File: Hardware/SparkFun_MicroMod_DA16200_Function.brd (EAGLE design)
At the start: 65 x 38 mm, 45 parts, among them J1 MICROMOD_STANDARD, J2 CORTEX_JTAG_DEBUG, U1 DA16200MOD, U2 CH340E_MSOP10, U3 3.3V

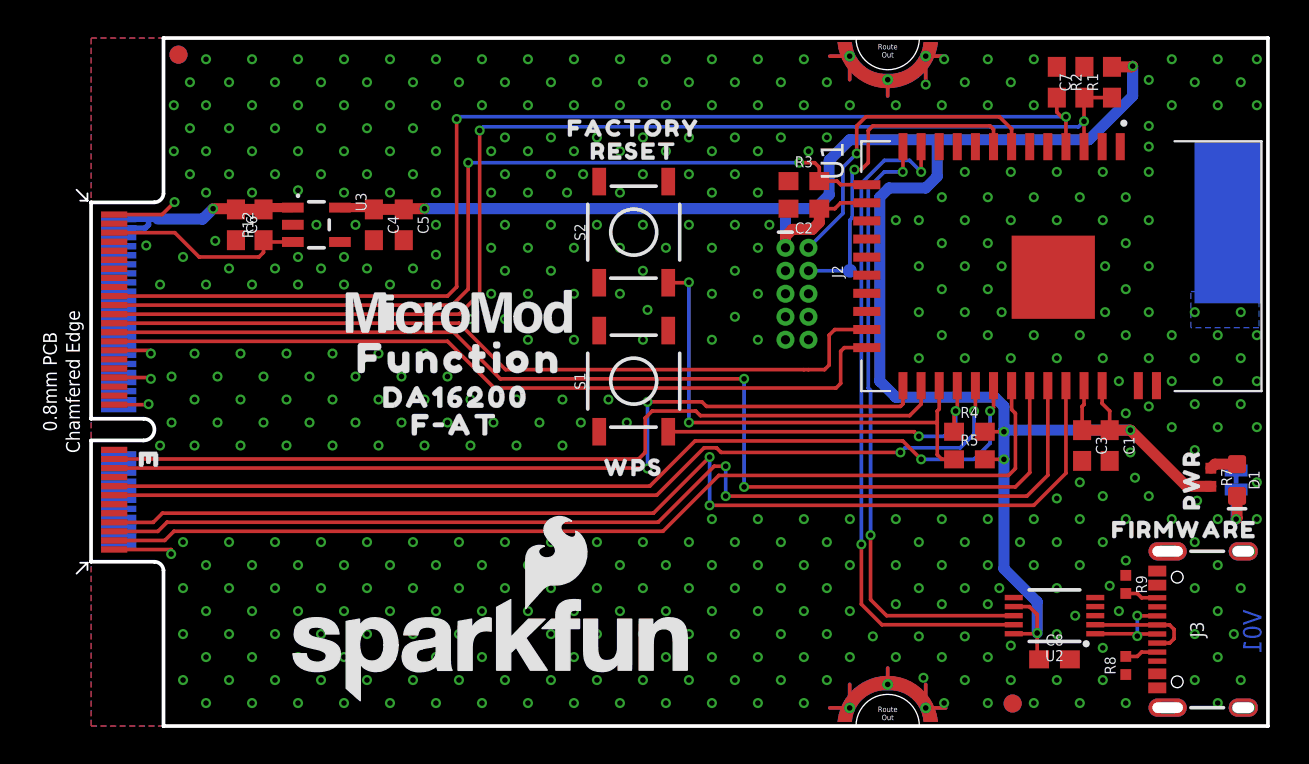
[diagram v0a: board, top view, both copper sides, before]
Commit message: Design Review Changes
Swapped U1RX/TX
Corrected SCL/SDA
Added a few more vias on the PCB
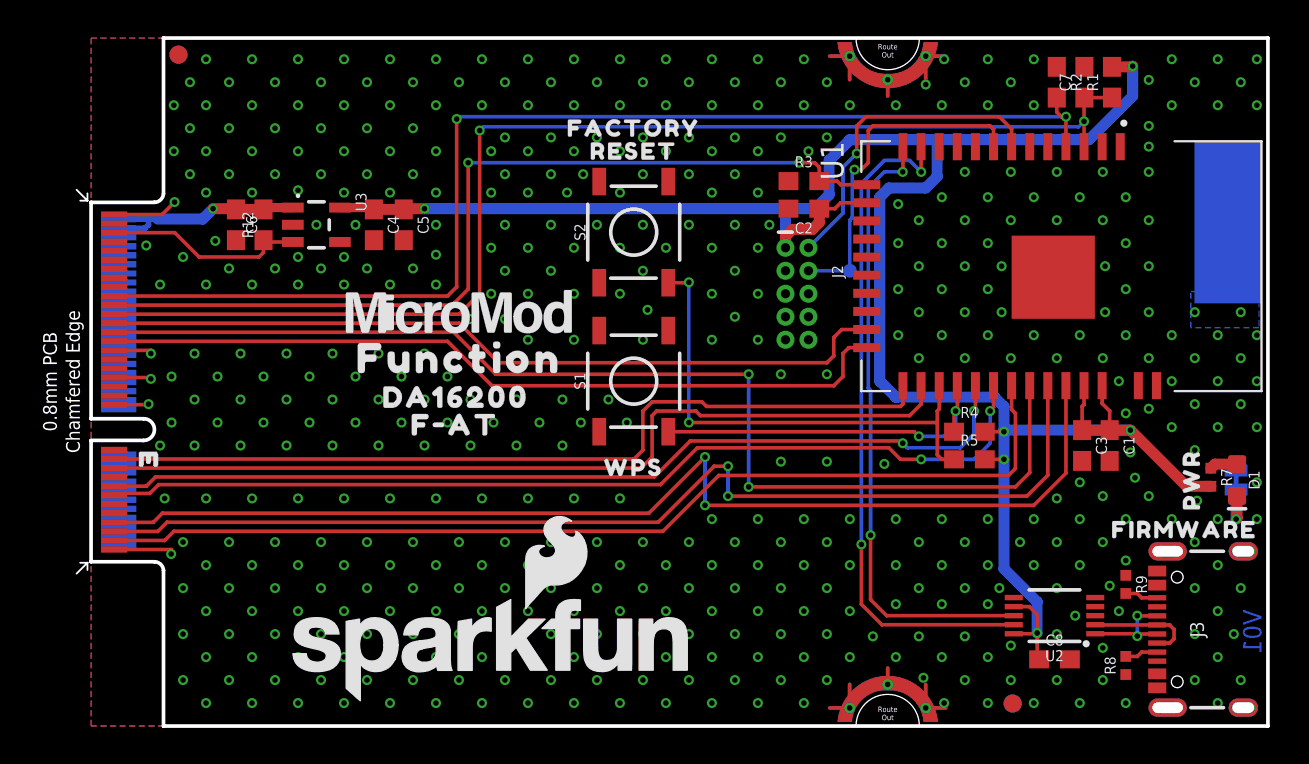
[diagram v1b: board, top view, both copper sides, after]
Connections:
- net CS renamed !CS!
- net SCL: now also J1.21; no longer J1.19
- net SDA: now also J1.19; no longer J1.21
- net U1RXI: now also J1.15; no longer J1.13
- net U1TXO: now also J1.13; no longer J1.15
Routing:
- net SCL: track 48.4 -> 47.3 mm, vias 2 -> 0
- net GPIOA11: track 44.5 -> 43.8 mm
- net GND: vias 476 -> 495

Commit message: Added Ordering Instructions
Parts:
- added LOGO3: SPECIAL_INSTRUCTIONS-ORDERING, SparkFun-Aesthetics:ORDERING_INSTRUCTIONS
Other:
- board text added: "0.8mm PCB ENIG Finish 45 degree chamfered edge"
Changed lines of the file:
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@@
 <dimension x1="4" y1="38" x2="65" y2="38" x3="34.5" y3="41" textsize="1.016" textratio="15" layer="47"/>
 <dimension x1="0" y1="9.075" x2="65" y2="9" x3="32.486146875" y3="-2.969409375" textsize="1.016" textratio="15" layer="47" visible="yes"/>
+<text x="86.36" y="29.21" size="1.778" layer="51" font="vector" ratio="15">0.8mm PCB
+ENIG Finish
+45 degree chamfered edge</text>
 </plain>
 <attributes>
@@
 <attribute name="VALUE" x="16.51" y="27.686" size="0.6096" layer="27" font="vector" ratio="20" rot="R270" align="top-center"/>
 </element>
+<element name="LOGO3" library="SparkFun-Aesthetics" package="ORDERING_INSTRUCTIONS" value="SPECIAL_INSTRUCTIONS-ORDERING" x="85.09" y="46.99" smashed="yes"/>
 </elements>
 <signals>

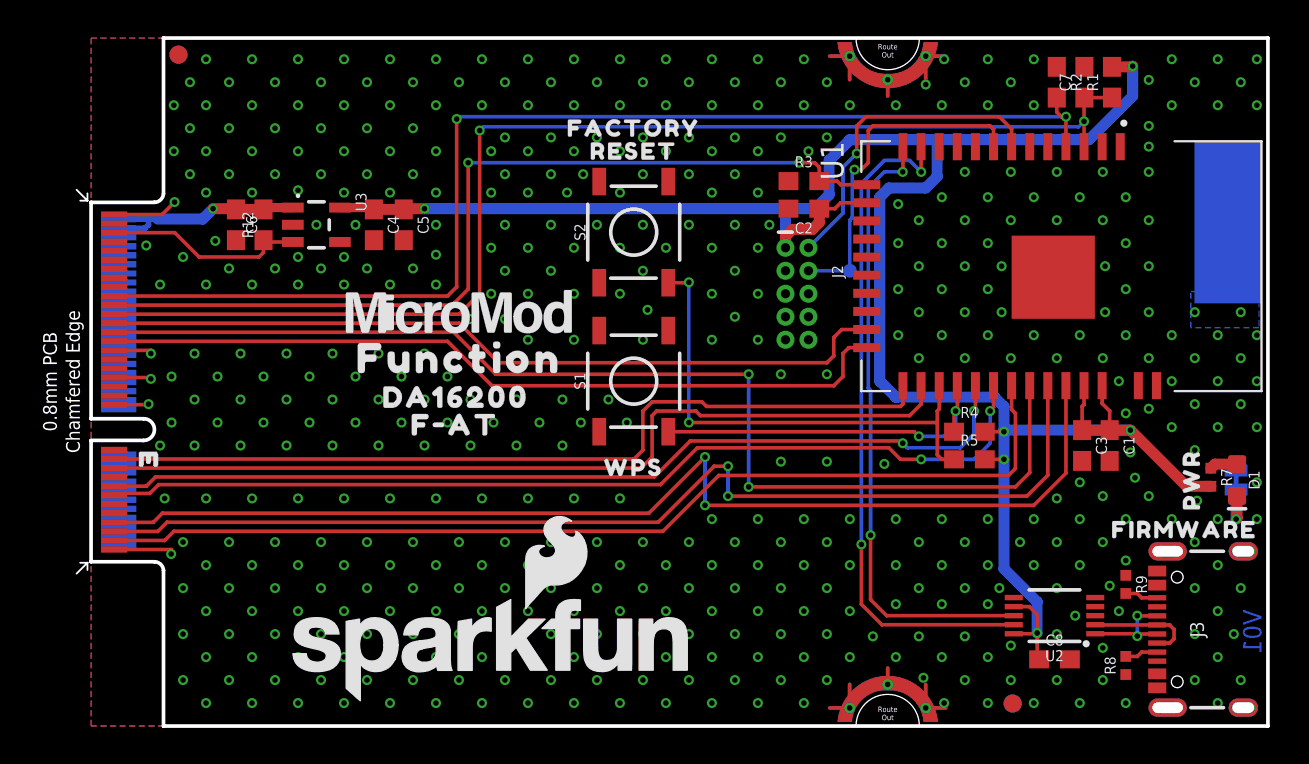
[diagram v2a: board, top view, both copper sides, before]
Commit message: V10
Added EEPROM, I2C Pullups
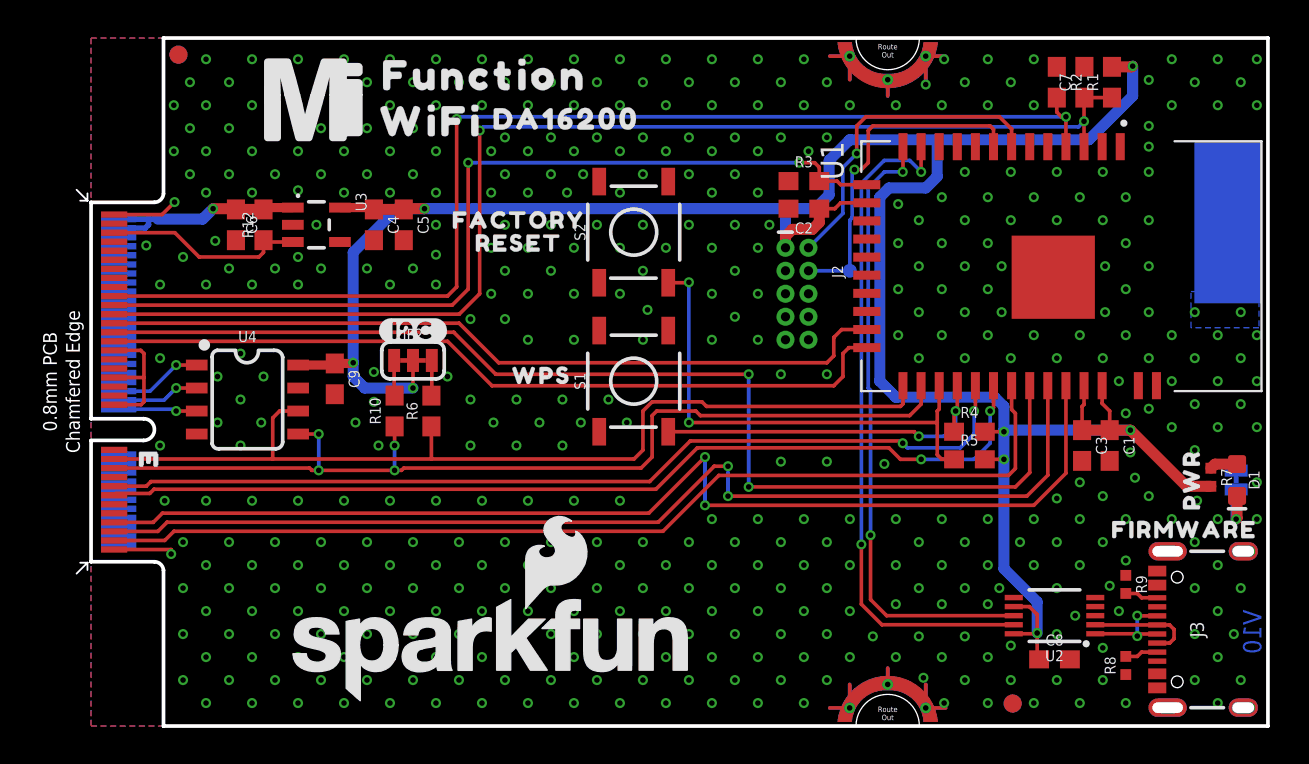
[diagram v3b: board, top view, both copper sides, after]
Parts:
- removed FRAME1: FRAME-LETTER, SparkFun-Aesthetics:CREATIVE_COMMONS
- removed U$10: (no value), SparkFun-MicroMod:MICROMOD_LOGO_.5
- added C9: 0.1uF, SparkFun-Capacitors:0603
- added FRAME2: FRAME-LEDGER, SparkFun-Aesthetics:CREATIVE_COMMONS
- added JP2: JUMPER-SMT_3_2-NC_TRACE_SILK, SparkFun-Jumpers:SMT-JUMPER_3_2-NC_TRACE_SILK
- added R10, R6: 4.7k, SparkFun-Resistors:0603
- added U$11: (no value), output:#I2C#0
- added U$12: (no value), SparkFun-MicroMod:MICROMOD_MI_LOGO_1
- added U4: EEPROM, SparkFun-IC-Memory:SO08
- U$6: device output:F#AT0 -> output:WIFI0
- moved U$6 16.8 mm to (18.8, 33.4)
- moved U$5 16.5 mm to (26.2, 33.5)
- moved U$4 15.7 mm to (21.7, 35.9)
- moved U$8 8.13 mm to (23.6, 27.9)
- moved U$9 8.13 mm to (23.6, 26.7)
- moved LOGO3 8.03 mm to (77.5, 44.5)
- moved U$7 7.18 mm to (24.9, 19.4)
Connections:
- removed net SCL: J1.21, U1.24
- removed net SDA: J1.19, U1.25
- new net I2C_SCL: J1.21, R6.1, U1.24, U4.6
- new net I2C_SDA: J1.19, R10.1, U1.25, U4.5
- new net N$1: J1.36, U4.1
- new net N$13: JP2.1, R10.2
- new net N$14: JP2.3, R6.2
- new net N$8: J1.32, U4.3
- new net N$9: J1.34, U4.2
- net 3.3V: now also C9.1, JP2.2, U4.8
- net GND: now also C9.2, U4.4, U4.7
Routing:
- net I2C_SDA: track 0.00 -> 54.3 mm, vias 0 -> 4
- net I2C_SCL: track 0.00 -> 52.9 mm
- net SDA: track 48.6 -> 0.00 mm
- net SCL: track 47.3 -> 0.00 mm
- net 3.3V: track 123.4 -> 143.5 mm, vias 6 -> 8
- net N$1: track 0.00 -> 4.91 mm, vias 0 -> 1
- net N$9: track 0.00 -> 4.59 mm, vias 0 -> 1
- net N$8: track 0.00 -> 4.35 mm, vias 0 -> 1
- net N$14: track 0.00 -> 1.97 mm
- net N$13: track 0.00 -> 1.97 mm
- net GND: track 24.6 -> 26.1 mm, vias 495 -> 470
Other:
- board text added: "V10"
- board text removed: "V01"

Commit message: V10 update
Added diodes for VIN and VUSB
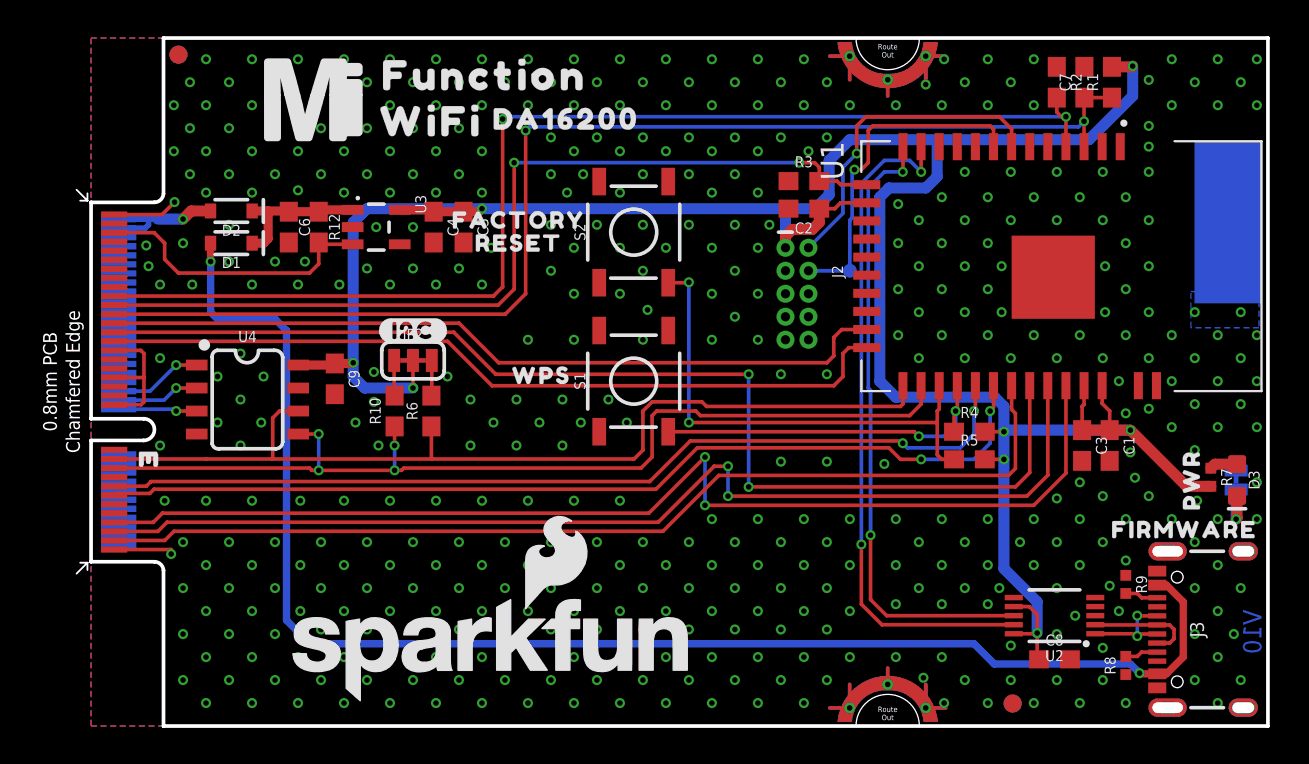
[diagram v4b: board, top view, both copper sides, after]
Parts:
- added D2: (no value), SparkFun-DiscreteSemi:SOD-323
- added D3: RED, SparkFun-MicroMod-Function:LED-0603
- D1: value RED -> (none); device SparkFun-MicroMod-Function:LED-0603 -> SparkFun-DiscreteSemi:SOD-323
- moved D1 57.1 mm to (7.75, 26.7), turned to 180 degrees
- moved C5 3.30 mm to (20.6, 27.6)
- moved U3 3.30 mm to (15.7, 27.6)
- moved C4 3.30 mm to (18.9, 27.6)
- moved R12 3.05 mm to (12.6, 27.6), turned to 270 degrees
- moved C6 2.92 mm to (10.9, 27.6)
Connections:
- new net N$3: C6.1, D1.C, D2.C, R12.1, U3.1
- new net V_USB: D1.A, J3.VBUS1, J3.VBUS2
- net EN: now also R12.2; no longer R12.1
- net N$6: now also D3.C; no longer D1.C
- net N$7: now also D3.A; no longer D1.A
- net VCC: now also D2.A; no longer C6.1, R12.2, U3.1
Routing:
- net V_USB: track 0.00 -> 80.4 mm, vias 0 -> 2
- net N$3: track 0.00 -> 8.12 mm
- net EN: track 11.2 -> 16.1 mm
- net VCC: track 12.0 -> 7.30 mm
- net 3.3V: track 143.5 -> 144.4 mm
- net GND: vias 470 -> 459

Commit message: V10 EEPROM changes
Added pullup, jumper, and MM pin map for EEPROM WP pin
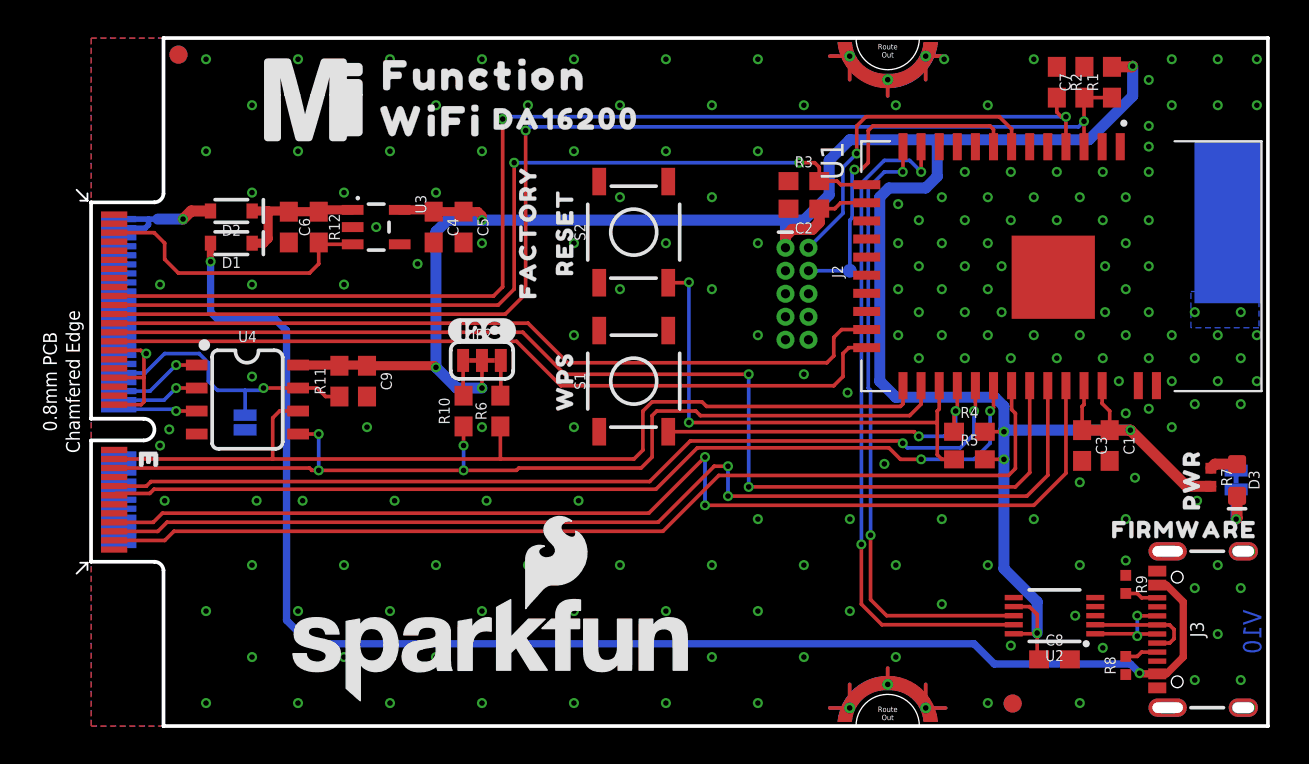
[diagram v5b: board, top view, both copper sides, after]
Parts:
- added JP3: (no value), SparkFun-Jumpers:SMT-JUMPER_2_NO_SILK
- added R11: 10k, SparkFun-Resistors:0603
- added U$10: (no value), output:#WP#0
- moved R10 3.81 mm to (20.6, 17.4)
- moved R6 3.81 mm to (22.6, 17.4)
- moved JP2 3.81 mm to (21.6, 20.2)
- moved U$11 3.81 mm to (21.6, 21.8)
- moved U$9 2.61 mm to (26.2, 27.3), turned to 90 degrees
- moved C9 1.78 mm to (15.2, 19.1)
- moved U$7 1.31 mm to (26.2, 19.1), turned to 90 degrees
- moved U$8 0.83 mm to (24.1, 27.3), turned to 90 degrees
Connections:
- new net EWP: J1.40, JP3.2, R11.1, U4.7
- net 3.3V: now also R11.2
- net GND: now also JP3.1; no longer U4.7
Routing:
- net EWP: track 0.00 -> 15.7 mm, vias 0 -> 1
- net GND: track 26.1 -> 19.1 mm, vias 459 -> 185
- net 3.3V: track 144.4 -> 142.6 mm

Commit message: Updates function board symbol, fixes text that was not vector
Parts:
- JP3: value (none) -> JUMPER-SMT_2_NO_SILK
- R1: value DNP -> (none)
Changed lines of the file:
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@@
 <drawing>
 <settings>
-<setting alwaysvectorfont="yes"/>
+<setting alwaysvectorfont="no"/>
 <setting verticaltext="up"/>
 </settings>
-<grid distance="0.05" unitdist="inch" unit="inch" style="lines" multiple="1" display="yes" altdistance="0.005" altunitdist="inch" altunit="inch"/>
+<grid distance="0.05" unitdist="inch" unit="inch" style="dots" multiple="1" display="yes" altdistance="0.005" altunitdist="inch" altunit="inch"/>
 <layers>
 <layer number="1" name="Top" color="4" fill="1" visible="yes" active="yes"/>
@@
 <layer number="14" name="Route14" color="22" fill="1" visible="no" active="no"/>
 <layer number="15" name="Route15" color="23" fill="1" visible="no" active="no"/>
-<layer number="16" name="Bottom" color="1" fill="1" visible="yes" active="yes"/>
-<layer number="17" name="Pads" color="2" fill="1" visible="yes" active="yes"/>
+<layer number="16" name="Bottom" color="3" fill="1" visible="yes" active="yes"/>
+<layer number="17" name="Pads" color="26" fill="1" visible="yes" active="yes"/>
 <layer number="18" name="Vias" color="2" fill="1" visible="yes" active="yes"/>
 <layer number="19" name="Unrouted" color="6" fill="1" visible="yes" active="yes"/>
-<layer number="20" name="Dimension" color="24" fill="1" visible="yes" active="yes"/>
+<layer number="20" name="Dimension" color="15" fill="1" visible="yes" active="yes"/>
 <layer number="21" name="tPlace" color="16" fill="1" visible="yes" active="yes"/>
 <layer number="22" name="bPlace" color="14" fill="1" visible="yes" active="yes"/>
@@
 <layer number="37" name="tTest" color="7" fill="1" visible="no" active="yes"/>
 <layer number="38" name="bTest" color="7" fill="1" visible="no" active="yes"/>
-<layer number="39" name="tKeepout" color="4" fill="11" visible="yes" active="yes"/>
+<layer number="39" name="tKeepout" color="4" fill="11" visible="no" active="yes"/>
 <layer number="40" name="bKeepout" color="1" fill="11" visible="no" active="yes"/>
 <layer number="41" name="tRestrict" color="4" fill="10" visible="no" active="yes"/>
@@
 <layer number="43" name="vRestrict" color="2" fill="10" visible="no" active="yes"/>
 <layer number="44" name="Drills" color="7" fill="1" visible="no" active="yes"/>
-<layer number="45" name="Holes" color="7" fill="1" visible="no" active="yes"/>
+<layer number="45" name="Holes" color="7" fill="1" visible="yes" active="yes"/>
 <layer number="46" name="Milling" color="3" fill="1" visible="no" active="yes"/>
-<layer number="47" name="Measures" color="7" fill="1" visible="yes" active="yes"/>
+<layer number="47" name="Measures" color="7" fill="1" visible="no" active="yes"/>
 <layer number="48" name="Document" color="7" fill="1" visible="no" active="yes"/>
-<layer number="49" name="Reference" color="7" fill="1" visible="no" active="yes"/>
+<layer number="49" name="Reference" color="13" fill="1" visible="yes" active="yes"/>
 <layer number="50" name="dxf" color="7" fill="1" visible="no" active="no"/>
 <layer number="51" name="tDocu" color="6" fill="1" visible="yes" active="yes"/>
@@
 </element>
 <element name="TP1" library="SparkFun-Connectors" package="PAD.03X.03" value="" x="41.91" y="25.146" smashed="yes" rot="MR0"/>
-<element name="R1" library="SparkFun-Resistors" package="0603" value="DNP" x="56.388" y="35.56" smashed="yes" rot="R90">
+<element name="R1" library="SparkFun-Resistors" package="0603" value=" " x="56.388" y="35.56" smashed="yes" rot="R90">
 <attribute name="NAME" x="55.626" y="35.56" size="0.6096" layer="25" font="vector" ratio="20" rot="R90" align="bottom-center"/>
 <attribute name="PROD_ID" value=" " x="57.658" y="15.24" size="1.778" layer="27" font="vector" ratio="15" rot="R90" display="off"/>
@@
 <attribute name="VALUE" x="14.478" y="19.05" size="0.6096" layer="27" font="vector" ratio="20" rot="R90" align="top-center"/>
 </element>
-<element name="JP3" library="SparkFun-Jumpers" package="SMT-JUMPER_2_NO_SILK" package3d_urn="urn:adsk.eagle:package:39279/1" value="" x="8.509" y="16.764" smashed="yes" rot="MR90">
+<element name="JP3" library="SparkFun-Jumpers" package="SMT-JUMPER_2_NO_SILK" package3d_urn="urn:adsk.eagle:package:39279/1" value="JUMPER-SMT_2_NO_SILK" x="8.509" y="16.764" smashed="yes" rot="MR90">
 <attribute name="NAME" x="9.652" y="16.764" size="0.6096" layer="26" font="vector" ratio="20" rot="MR90" align="bottom-center"/>
 <attribute name="VALUE" x="7.366" y="16.764" size="0.6096" layer="28" font="vector" ratio="20" rot="MR90" align="top-center"/>
